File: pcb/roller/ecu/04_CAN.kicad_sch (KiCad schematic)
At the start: 10 parts, among them U2 TJA1050DRG, U3 TJA1050DRG

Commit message: Add design settings and DRC rules to ECU PCB configuration
- Introduced comprehensive design settings including defaults for various parameters such as line widths, text sizes, and pad dimensions.
- Added detailed DRC (Design Rule Check) exclusions and rule severities to enhance error handling and warnings during PCB design.
- Updated tuning pattern settings and teardrop parameters for improved track and pad connections.
- Cleared previously used designators for better organization and clarity in the design file.
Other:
- note added: "PB12"
- note added: "PB13"
- note added: "PD0"
- note added: "PD1"

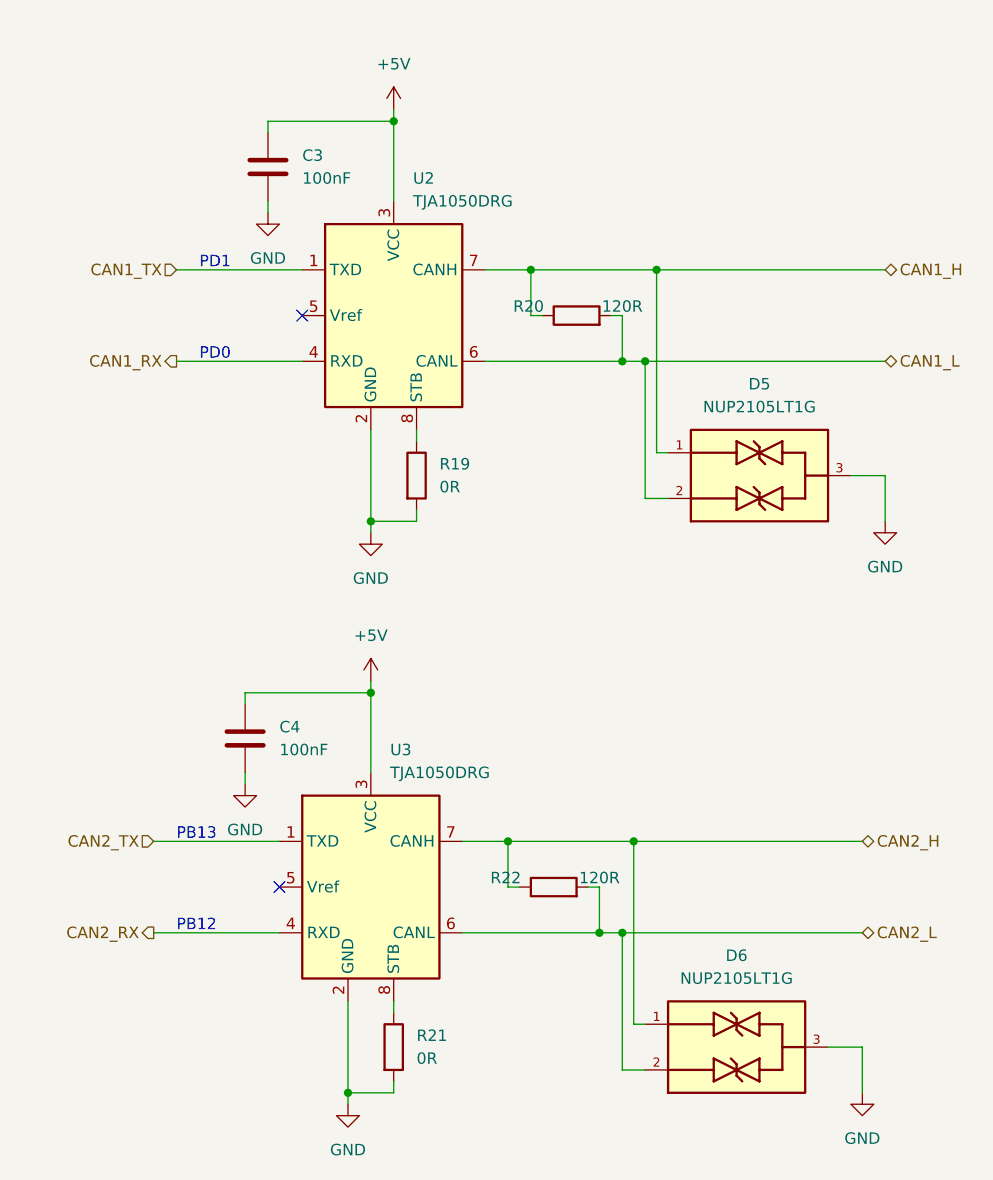
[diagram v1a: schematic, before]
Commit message: Add ESTOP_NC pin and wire connections in ECU schematic; update designators in PCB project
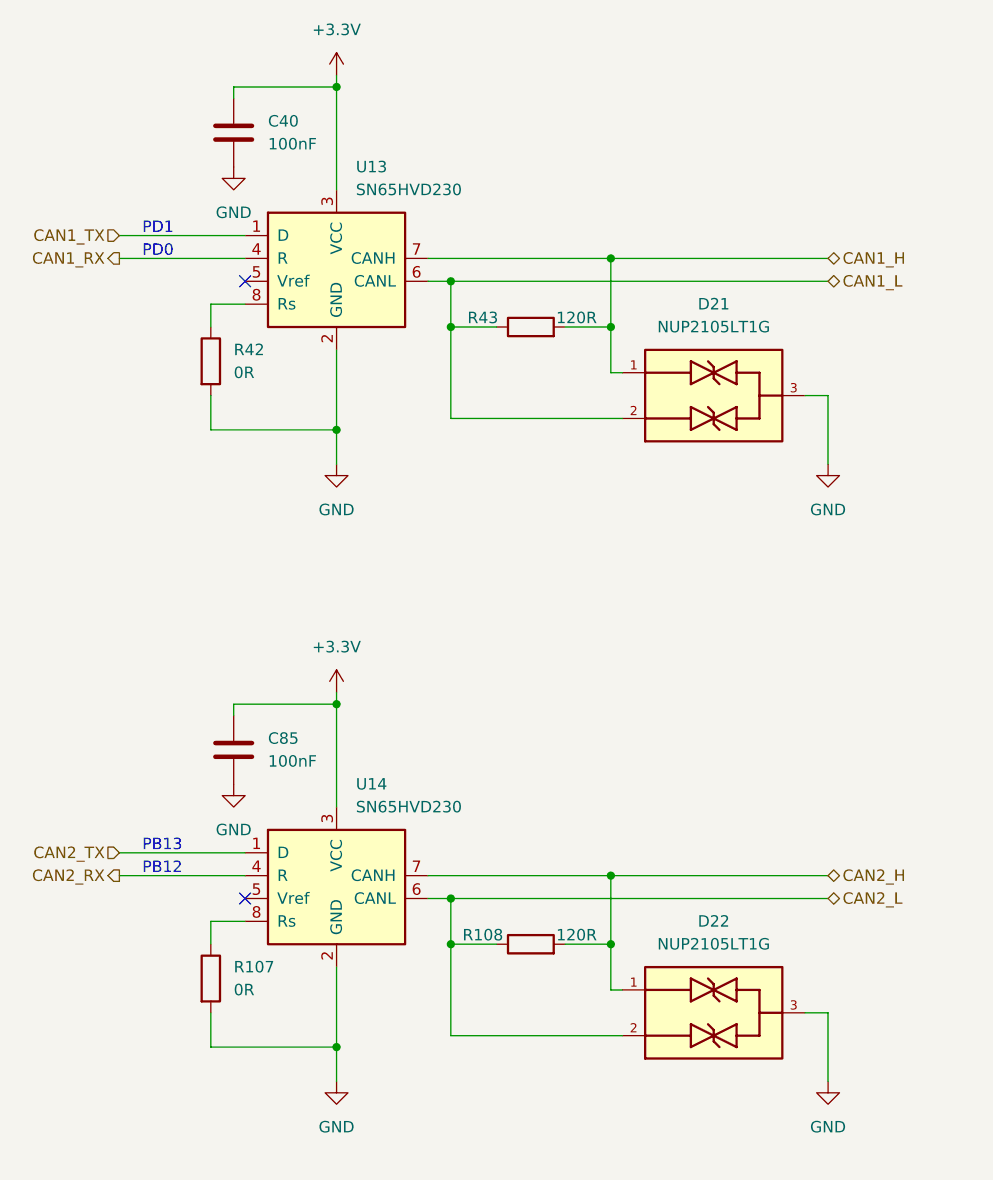
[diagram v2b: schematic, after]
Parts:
- removed C3, C4: 100nF, Capacitor_SMD:C_0603_1608Metric, symbol Device:C
- removed D5, D6: NUP2105LT1G, Starlight:SOT95P237X111-3N, symbol Starlight:NUP2105LT1G
- removed R19, R21: 0R, Resistor_SMD:R_0603_1608Metric, symbol Device:R
- removed R20, R22: 120R, Resistor_SMD:R_0603_1608Metric, symbol Device:R
- removed U2, U3: TJA1050DRG, Package_SO:SOIC-8_3.9x4.9mm_P1.27mm, symbol Starlight:TJA1050DRG
- added C40, C85: 100nF, Capacitor_SMD:C_0603_1608Metric, symbol Device:C
- added D21, D22: NUP2105LT1G, Starlight:SOT95P237X111-3N, symbol Starlight:NUP2105LT1G
- added R107, R42: 0R, Resistor_SMD:R_0603_1608Metric, symbol Device:R
- added R108, R43: 120R, Resistor_SMD:R_0603_1608Metric, symbol Device:R
- added U13, U14: SN65HVD230, Package_SO:SOIC-8_3.9x4.9mm_P1.27mm, symbol Interface_CAN_LIN:SN65HVD230
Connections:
- net CAN1_H: now also D21.1, R43.2, U13.7 (CANH)
- net CAN1_L: now also D21.2, R43.1, U13.6 (CANL)
- net CAN1_RX: now also U13.4 (R)
- net CAN1_TX: now also U13.1 (D)
- net CAN2_H: now also D22.1, R108.2, U14.7 (CANH)
- net CAN2_L: now also D22.2, R108.1, U14.6 (CANL)
- net CAN2_RX: now also U14.4 (R)
- net CAN2_TX: now also U14.1 (D)
- net GND: now also C40.2, C85.2, D21.3, D22.3, R107.2, R42.2, U13.2 (GND), U14.2 (GND)
- new net: R42.1, U13.8 (Rs)
- new net: R107.1, U14.8 (Rs)
- new net +3.3V: C40.1, C85.1, U13.3 (VCC), U14.3 (VCC)
